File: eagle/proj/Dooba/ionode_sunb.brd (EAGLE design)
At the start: 27.4 x 27.4 mm, 42 parts, among them J1 USB-BAMPHENOL-MICRO, U1 TPS61200S-PVSON-N10, U2 MAX1811SO8, U3 FT232RQFN32, U4 MCP4018SC70, U5 DIPSWITCH_2DIP, U6 AP7335SOT23-5

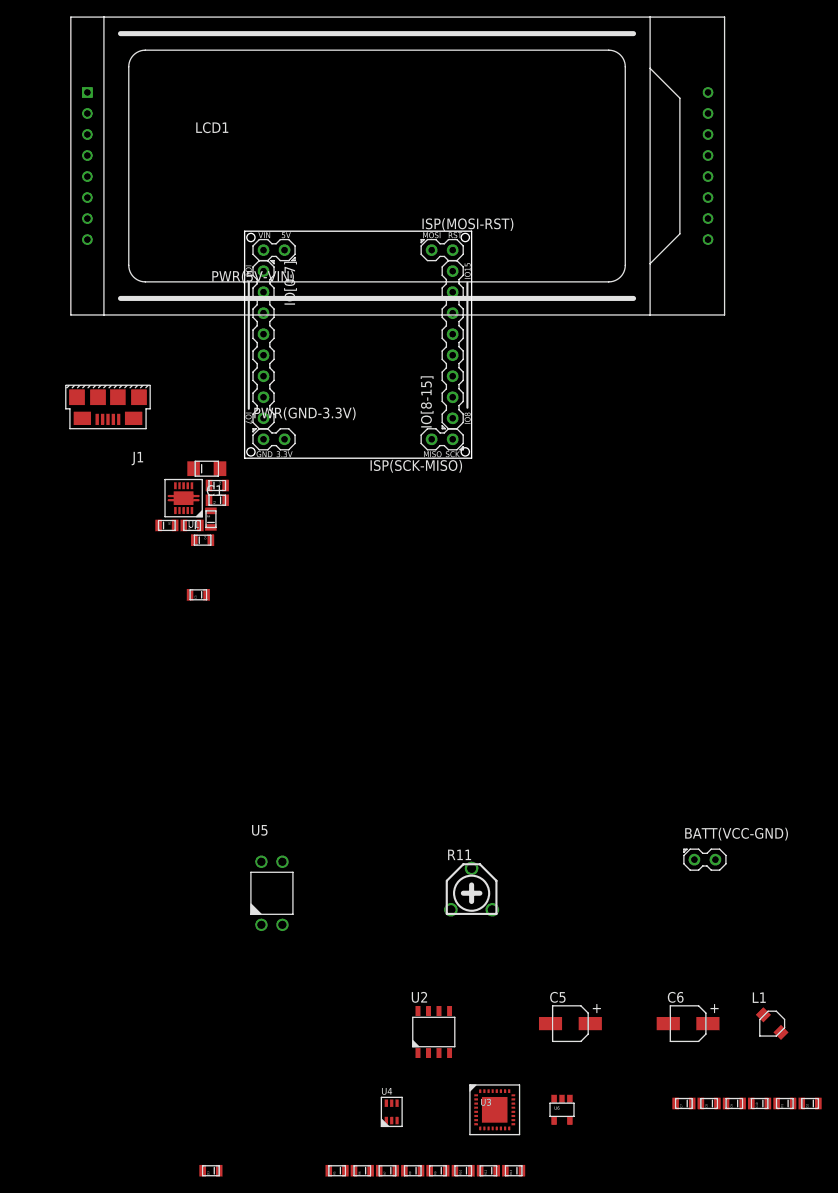
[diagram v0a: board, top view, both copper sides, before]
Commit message: Started shiva mp3 player board
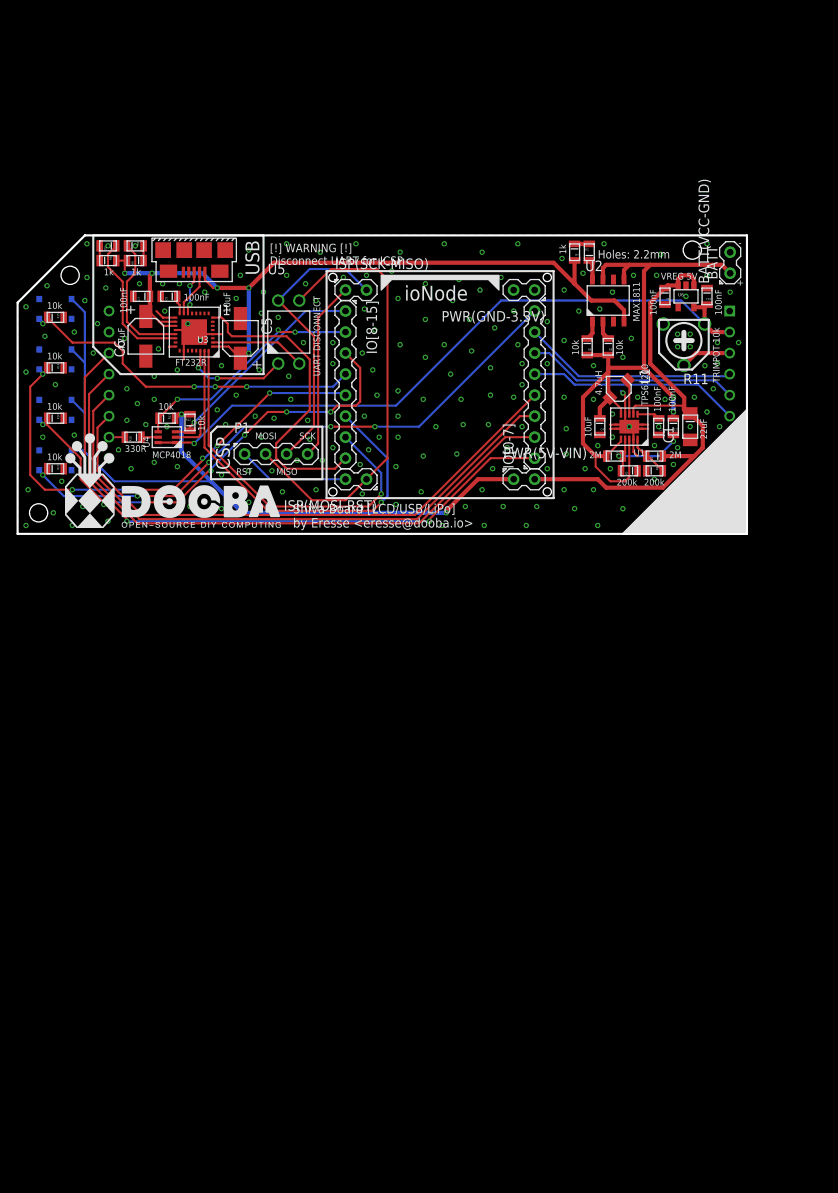
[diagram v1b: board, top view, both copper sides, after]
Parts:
- added P1: ICSP(RST-MOSI-MISO-SCK), dooba:PIN_4
- added R14, R15, R16, R17: 10k, dooba:0805
- added SW1, SW2, SW3, SW4: TACTSWCK_PTS_830, dooba:TACTSW_CK_PTS_830
- R11: value TRIMPOTBOURNS-3306F -> LCD_CONTRAST
- U5: value DIPSWITCH_2DIP -> UART_DCNT
- moved D2 133.9 mm to (18.0, 61.5)
- moved C7 117.5 mm to (22.1, 55.4)
- moved C8 117.4 mm to (25.4, 55.4)
- moved R8 116.0 mm to (18.0, 59.7), turned to 180 degrees
- moved R9 115.9 mm to (21.3, 59.7)
- moved R7 113.3 mm to (74.4, 60.7), turned to 90 degrees
- moved D3 112.1 mm to (21.3, 61.5), turned to 180 degrees
- moved C6 105.8 mm to (22.6, 50.5), turned to 90 degrees
- moved D1 105.5 mm to (76.2, 60.7), turned to 270 degrees
- moved R5 104.8 mm to (78.5, 49.3), turned to 90 degrees
- moved R6 103.2 mm to (75.9, 49.3), turned to 90 degrees
- moved U3 100.8 mm to (28.4, 51.1), turned to 180 degrees
- moved R13 100.1 mm to (25.1, 40.6), turned to 180 degrees
- moved U6 99.4 mm to (87.9, 55.4)
- moved C9 97.9 mm to (85.3, 55.4), turned to 90 degrees
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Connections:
- new net N$21: IO[8-15].5, R14.2, SW1.4
- new net N$22: IO[8-15].4, R15.2, SW2.4
- new net N$23: IO[8-15].3, R16.2, SW3.4
- new net N$24: IO[0-7].8, R17.2, SW4.4
- new net N$25: ISP(SCK-MISO).1, P1.4
- new net N$26: ISP(MOSI-RST).2, P1.1
- net GND: now also R14.1, R15.1, R16.1, R17.1, U1.PAD0, U1.PAD1, U1.PAD2, U1.PAD3
- net LCD_BACKLIGHT_SCL: now also R12.2
- net LCD_BACKLIGHT_SDA: no longer R12.2
- net N$1: now also P1.2
- net N$16: now also P1.3
- net VCC: now also SW1.1, SW2.1, SW3.1, SW4.1
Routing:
- net USBVCC: track 0.00 -> 99.0 mm, vias 0 -> 5
- net VCC: track 0.00 -> 93.6 mm, vias 0 -> 2
- net BATTVCC: track 0.00 -> 84.4 mm, vias 0 -> 2
- net LCDVCC: track 0.00 -> 81.6 mm, vias 0 -> 1
- net LCD_D4: track 0.00 -> 76.2 mm, vias 0 -> 2
- net LCD_D5: track 0.00 -> 73.8 mm
- net N$24: track 0.00 -> 71.5 mm, vias 0 -> 5
- net LCD_D6: track 0.00 -> 71.0 mm
- net LCD_D7: track 0.00 -> 68.2 mm
- net VIN: track 0.00 -> 63.2 mm
- net N$21: track 0.00 -> 58.5 mm, vias 0 -> 6
- net N$23: track 0.00 -> 57.6 mm, vias 0 -> 7
- net N$1: track 0.00 -> 53.5 mm
- net DTR: track 0.00 -> 49.5 mm, vias 0 -> 1
- net RTS: track 0.00 -> 44.6 mm, vias 0 -> 1
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- added copper zone on layer 1, net GND
- added copper zone on layer 16, net GND
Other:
- board size 27.4 x 27.4 mm -> 88.1 x 36.1 mm
- board text added: "+"
- board text added: "-"
- board text added: "100nF"
- board text added: "10k"
- board text added: "10uF"
- board text added: "1k"
- board text added: "200k"
- board text added: "22uF"
- board text added: "2M"
- board text added: "330R"
- board text added: "4.7uF"
- board text added: "4.7uH"
- board text added: "4x20 Text LCD"
- board text added: "BATT"
- board text added: "FT232R"
- board text added: "Holes: 2.2mm"
- board text added: "ICSP"
- board text added: "MAX1811"
- board text added: "MCP4018"
- board text added: "Shiva Board [LCD/USB/LiPo] by Eresse <eresse@dooba.io>"
- board text added: "TPS61200"
- board text added: "TRIMPOT 10k"
- board text added: "UART DISCONNECT"
- board text added: "USB"
- board text added: "VREG 5V"
- board text added: "[!] WARNING [!] Disconnect UART for ICSP"
- board text added: "ioNode"
- board text removed: "3.3V"
- board text removed: "5V"
- board text removed: "GND"
- board text removed: "IO0"
- board text removed: "IO15"
- board text removed: "IO7"
- board text removed: "IO8"
- board text removed: "VIN"
